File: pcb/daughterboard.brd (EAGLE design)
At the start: 28 x 24 mm, 27 parts, among them IC3 STM32F042F4, SW1 324_SW, SW2 324_SW, SW4 324_SW, SW5 324_SW, SW6 324_SW, U4 XC6206_DEV

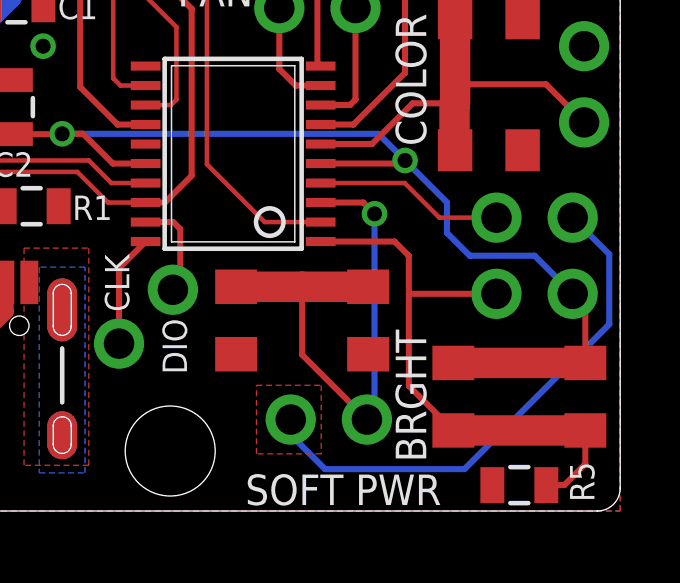
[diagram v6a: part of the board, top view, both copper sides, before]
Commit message: moved pin headers to the outer edge
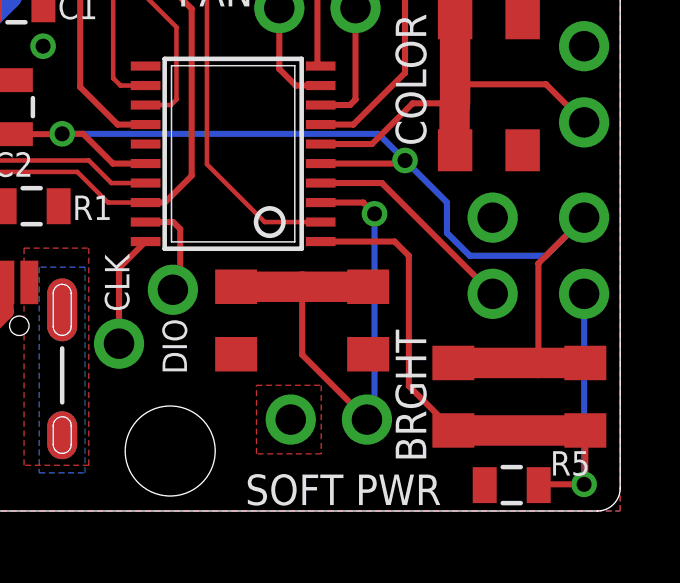
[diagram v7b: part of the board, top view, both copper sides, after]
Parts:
- moved U$4 2.08 mm to (26.8, 8.51), turned to 270 degrees
- moved U$8 1.89 mm to (23.7, 8.51), turned to 90 degrees
- moved R5 0.25 mm to (24.4, 0.86)
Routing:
- net GND: track 29.5 -> 11.8 mm
- net BUTTON2: track 19.6 -> 23.7 mm, vias 0 -> 1
- net +3V3: track 38.6 -> 42.0 mm
- net BUTTON1: track 6.34 -> 7.26 mm
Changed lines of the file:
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@@
 <attribute name="NAME" x="5.1689" y="21.3614" size="0.8128" layer="25" rot="R270"/>
 </element>
-<element name="R5" library="joyAnalog" package="0805" value="5K1" x="24.638" y="0.8636" smashed="yes">
-<attribute name="NAME" x="27.1399" y="0.3048" size="0.8128" layer="25" rot="R90"/>
+<element name="R5" library="joyAnalog" package="0805" value="5K1" x="24.384" y="0.8636" smashed="yes">
+<attribute name="NAME" x="27.0002" y="1.9939" size="0.8128" layer="25" rot="R180"/>
 </element>
 <element name="U4" library="3pos_slide_switch" package="SOT23R_INFINEON" value="XC6206_DEV" x="2.667" y="13.462" smashed="yes"/>
@@
 <element name="U$2" library="adafruit_changed" package="1X02" value="PINHD1X2" x="24.638" y="22.86" smashed="yes"/>
 <element name="U$3" library="adafruit_changed" package="1X02" value="PINHD1X2" x="26.797" y="14.224" smashed="yes" rot="R90"/>
-<element name="U$4" library="adafruit_changed" package="1X02" value="PINHD1X2" x="25.146" y="7.239" smashed="yes" rot="R180"/>
+<element name="U$4" library="adafruit_changed" package="1X02" value="PINHD1X2" x="26.797" y="8.509" smashed="yes" rot="R270"/>
 <element name="SW1" library="3pos_slide_switch_centered" package="342_SWICH_FOOT" value="324_SW" x="17.399" y="19.812" smashed="yes"/>
 <element name="SW2" library="3pos_slide_switch_centered" package="342_SWICH_FOOT" value="324_SW" x="24.638" y="19.812" smashed="yes" rot="R180"/>
@@
 <attribute name="NAME" x="4.0005" y="14.351" size="0.8128" layer="25" rot="R90"/>
 </element>
-<element name="U$8" library="adafruit_changed" package="1X02" value="PINHD1X2" x="25.146" y="9.779" smashed="yes"/>
+<element name="U$8" library="adafruit_changed" package="1X02" value="PINHD1X2" x="23.749" y="8.509" smashed="yes" rot="R90"/>
 </elements>
 <signals>
@@
 <wire x1="13.716" y1="22.86" x2="13.716" y2="20.701" width="0.1524" layer="1"/>
 <wire x1="13.716" y1="20.701" x2="15.199" y2="19.218" width="0.1524" layer="1"/>
-<wire x1="26.416" y1="9.779" x2="27.6352" y2="8.5598" width="0.2032" layer="16"/>
-<wire x1="27.6352" y1="8.5598" x2="27.6352" y2="6.223" width="0.2032" layer="16"/>
-<wire x1="27.6352" y1="6.223" x2="22.8092" y2="1.397" width="0.2032" layer="16"/>
-<wire x1="18.161" y1="1.397" x2="17.018" y2="2.54" width="0.2032" layer="16"/>
-<wire x1="17.018" y1="2.54" x2="17.018" y2="3.048" width="0.2032" layer="16"/>
-<wire x1="22.8092" y1="1.397" x2="18.161" y2="1.397" width="0.2032" layer="16"/>
 </signal>
 <signal name="+3V3">
@@
 <wire x1="20.828" y1="11.684" x2="22.225" y2="10.287" width="0.2032" layer="16"/>
 <wire x1="22.225" y1="10.287" x2="22.225" y2="9.271" width="0.2032" layer="16"/>
-<wire x1="26.838" y1="4.935" x2="22.438" y2="4.935" width="1.016" layer="1"/>
-<wire x1="26.416" y1="7.239" x2="26.838" y2="6.817" width="0.2032" layer="1"/>
-<wire x1="26.838" y1="6.817" x2="26.838" y2="4.935" width="0.2032" layer="1"/>
+<wire x1="26.838" y1="4.935" x2="25.273" y2="4.935" width="1.016" layer="1"/>
+<wire x1="25.273" y1="4.935" x2="22.438" y2="4.935" width="1.016" layer="1"/>
 <wire x1="22.225" y1="9.271" x2="22.987" y2="8.509" width="0.2032" layer="16"/>
-<wire x1="25.146" y1="8.509" x2="26.416" y2="7.239" width="0.2032" layer="16"/>
-<wire x1="22.987" y1="8.509" x2="25.146" y2="8.509" width="0.2032" layer="16"/>
+<wire x1="22.987" y1="8.509" x2="25.527" y2="8.509" width="0.2032" layer="16"/>
+<wire x1="25.527" y1="8.509" x2="26.797" y2="9.779" width="0.2032" layer="16"/>
+<wire x1="26.797" y1="9.779" x2="25.273" y2="8.255" width="0.2032" layer="1"/>
+<wire x1="25.273" y1="8.255" x2="25.273" y2="4.935" width="0.2032" layer="1"/>
 </signal>
 <signal name="USB_DP">
@@
 <contactref element="IC3" pad="4"/>
 <contactref element="U$8" pad="1"/>
-<wire x1="21.971" y1="9.779" x2="23.876" y2="9.779" width="0.1524" layer="1"/>
-<wire x1="18.0168" y1="10.932" x2="20.818" y2="10.932" width="0.1524" layer="1"/>
-<wire x1="20.818" y1="10.932" x2="21.971" y2="9.779" width="0.1524" layer="1"/>
+<wire x1="18.0168" y1="10.932" x2="20.056" y2="10.932" width="0.2032" layer="1"/>
+<wire x1="20.056" y1="10.932" x2="23.749" y2="7.239" width="0.2032" layer="1"/>
 </signal>
 <signal name="BUTTON2">
@@
 <wire x1="20.955" y1="4.168" x2="22.438" y2="2.685" width="0.2032" layer="1"/>
 <wire x1="18.0168" y1="8.982" x2="20.482" y2="8.982" width="0.2032" layer="1"/>
-<wire x1="20.955" y1="8.509" x2="20.955" y2="7.239" width="0.2032" layer="1"/>
-<wire x1="20.955" y1="7.239" x2="20.955" y2="4.168" width="0.2032" layer="1"/>
+<wire x1="20.955" y1="8.509" x2="20.955" y2="4.168" width="0.2032" layer="1"/>
 <wire x1="20.482" y1="8.982" x2="20.955" y2="8.509" width="0.2032" layer="1"/>
-<wire x1="23.876" y1="7.239" x2="20.955" y2="7.239" width="0.2032" layer="1"/>
-<wire x1="26.838" y1="2.685" x2="26.838" y2="1.565" width="0.2032" layer="1"/>
-<wire x1="26.1366" y1="0.8636" x2="25.538" y2="0.8636" width="0.2032" layer="1"/>
-<wire x1="26.838" y1="1.565" x2="26.1366" y2="0.8636" width="0.2032" layer="1"/>
+<wire x1="26.797" y1="7.239" x2="26.797" y2="0.889" width="0.2032" layer="16"/>
+<via x="26.797" y="0.889" extent="1-16" drill="0.5"/>
+<wire x1="26.797" y1="0.889" x2="25.3094" y2="0.889" width="0.2032" layer="1"/>
+<wire x1="25.3094" y1="0.889" x2="25.284" y2="0.8636" width="0.2032" layer="1"/>
+<wire x1="26.838" y1="2.685" x2="26.838" y2="0.93" width="0.2032" layer="1"/>
+<wire x1="26.838" y1="0.93" x2="26.797" y2="0.889" width="0.2032" layer="1"/>
 </signal>
 <signal name="N$29">

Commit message: freed up more space
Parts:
- moved U$2 2.96 mm to (26.8, 20.8), turned to 90 degrees
- moved SW2 1.44 mm to (23.6, 20.8), turned to 90 degrees
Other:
- board text added: "ATX4VC.com"
- board text added: "FAN SPD"
- board text added: "RGB COLOR"
- board text added: "RGB MODE"
- board text added: "dekuNukem PD1 APR23"
- board text removed: "ATX4VC.com dekuNukem"
- board text removed: "PD1 APR23"
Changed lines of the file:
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@@
 <grid distance="5" unitdist="mil" unit="mil" style="lines" multiple="1" display="no" altdistance="1" altunitdist="mil" altunit="mil"/>
 <layers>
-<layer number="1" name="Top" color="4" fill="1" visible="yes" active="yes"/>
+<layer number="1" name="Top" color="4" fill="1" visible="no" active="yes"/>
 <layer number="2" name="Route2" color="16" fill="1" visible="no" active="no"/>
 <layer number="3" name="Route3" color="17" fill="1" visible="no" active="no"/>
@@
 <layer number="19" name="Unrouted" color="6" fill="1" visible="yes" active="yes"/>
 <layer number="20" name="Dimension" color="24" fill="1" visible="yes" active="yes"/>
-<layer number="21" name="tPlace" color="7" fill="1" visible="yes" active="yes"/>
-<layer number="22" name="bPlace" color="7" fill="1" visible="yes" active="yes"/>
-<layer number="23" name="tOrigins" color="15" fill="1" visible="yes" active="yes"/>
+<layer number="21" name="tPlace" color="7" fill="1" visible="no" active="yes"/>
+<layer number="22" name="bPlace" color="7" fill="1" visible="no" active="yes"/>
+<layer number="23" name="tOrigins" color="15" fill="1" visible="no" active="yes"/>
 <layer number="24" name="bOrigins" color="15" fill="1" visible="yes" active="yes"/>
-<layer number="25" name="tNames" color="7" fill="1" visible="yes" active="yes"/>
+<layer number="25" name="tNames" color="7" fill="1" visible="no" active="yes"/>
 <layer number="26" name="bNames" color="7" fill="1" visible="yes" active="yes"/>
-<layer number="27" name="tValues" color="7" fill="1" visible="yes" active="yes"/>
-<layer number="28" name="bValues" color="7" fill="1" visible="yes" active="yes"/>
+<layer number="27" name="tValues" color="7" fill="1" visible="no" active="yes"/>
+<layer number="28" name="bValues" color="7" fill="1" visible="no" active="yes"/>
 <layer number="29" name="tStop" color="7" fill="3" visible="no" active="yes"/>
 <layer number="30" name="bStop" color="7" fill="6" visible="no" active="yes"/>
@@
 <layer number="37" name="tTest" color="7" fill="1" visible="no" active="yes"/>
 <layer number="38" name="bTest" color="7" fill="1" visible="no" active="yes"/>
-<layer number="39" name="tKeepout" color="4" fill="11" visible="yes" active="yes"/>
+<layer number="39" name="tKeepout" color="4" fill="11" visible="no" active="yes"/>
 <layer number="40" name="bKeepout" color="1" fill="11" visible="yes" active="yes"/>
-<layer number="41" name="tRestrict" color="4" fill="10" visible="yes" active="yes"/>
+<layer number="41" name="tRestrict" color="4" fill="10" visible="no" active="yes"/>
 <layer number="42" name="bRestrict" color="1" fill="10" visible="yes" active="yes"/>
 <layer number="43" name="vRestrict" color="2" fill="10" visible="no" active="yes"/>
@@
 <layer number="49" name="Reference" color="7" fill="1" visible="no" active="yes"/>
 <layer number="50" name="dxf" color="7" fill="1" visible="no" active="no"/>
-<layer number="51" name="tDocu" color="7" fill="1" visible="yes" active="yes"/>
-<layer number="52" name="bDocu" color="7" fill="1" visible="yes" active="yes"/>
+<layer number="51" name="tDocu" color="7" fill="1" visible="no" active="yes"/>
+<layer number="52" name="bDocu" color="7" fill="1" visible="no" active="yes"/>
 <layer number="53" name="tGND_GNDA" color="7" fill="1" visible="no" active="no"/>
 <layer number="54" name="bGND_GNDA" color="7" fill="1" visible="no" active="no"/>
@@
 <text x="9.92" y="15.763" size="1.778" layer="26" rot="MR180" align="center">ATX4VC
 MCU Board</text>
-<text x="21.604" y="19.928" size="1.27" layer="26" rot="MR180" align="center">ATX4VC.com
-dekuNukem</text>
 <hole x="13" y="2" drill="3" locked="yes"/>
 <circle x="13" y="2" radius="2.6" width="0" layer="41"/>
 <text x="14.5034" y="17.3274" size="1.016" layer="25" rot="R180" align="center">FAN</text>
-<text x="21.0266" y="19.9644" size="1.016" layer="25" rot="R270" align="center">MODE</text>
+<text x="21.1536" y="20.5994" size="1.016" layer="25" rot="R270" align="center">MODE</text>
 <text x="21.0266" y="14.3764" size="1.016" layer="25" rot="R270" align="center">COLOR</text>
 <text x="21.0266" y="3.8354" size="1.016" layer="25" rot="R270" align="center">BRGHT</text>
@@
 <text x="11.2314" y="7.5946" size="0.8128" layer="25" distance="10" rot="R90" align="center">CLK</text>
 <text x="13.1526" y="5.4864" size="0.8128" layer="25" distance="10" rot="R270" align="center">DIO</text>
-<text x="9.793" y="10.784" size="1.27" layer="26" rot="MR180" align="center">PD1 APR23</text>
-<text x="19.2024" y="15.2954" size="0.8128" layer="26" rot="MR180" align="center">TX</text>
-<text x="16.6624" y="15.2954" size="0.8128" layer="26" rot="MR180" align="center">DB</text>
+<text x="19.2024" y="18.3434" size="0.8128" layer="26" rot="MR180" align="center">TX</text>
+<text x="16.6624" y="18.3434" size="0.8128" layer="26" rot="MR180" align="center">DB</text>
+<text x="24.3286" y="14.3764" size="1.016" layer="26" rot="MR270" align="center">RGB
+COLOR</text>
+<text x="24.3124" y="20.9296" size="1.016" layer="26" rot="MR90" align="center">RGB
+MODE</text>
+<text x="17.4244" y="21.1374" size="1.016" layer="26" rot="MR180" align="center">FAN SPD</text>
+<text x="26.7254" y="4.0386" size="1.016" layer="26" rot="MR90" align="center">BRGHT</text>
+<text x="18.6436" y="1.0876" size="1.016" layer="26" distance="10" rot="MR0" align="center">SOFT PWR</text>
+<text x="9.892" y="10.298" size="1.27" layer="26" rot="MR0" align="center">dekuNukem
+PD1 APR23</text>
+<text x="5.348" y="0.878" size="1.27" layer="26" rot="MR180" align="center">ATX4VC.com</text>
 </plain>
 <attributes>
@@
 </element>
 <element name="U$1" library="adafruit_changed" package="1X02" value="PINHD1X2" x="17.399" y="22.86" smashed="yes"/>
-<element name="U$2" library="adafruit_changed" package="1X02" value="PINHD1X2" x="24.638" y="22.86" smashed="yes"/>
+<element name="U$2" library="adafruit_changed" package="1X02" value="PINHD1X2" x="26.797" y="20.828" smashed="yes" rot="R90"/>
 <element name="U$3" library="adafruit_changed" package="1X02" value="PINHD1X2" x="26.797" y="14.224" smashed="yes" rot="R90"/>
 <element name="U$4" library="adafruit_changed" package="1X02" value="PINHD1X2" x="26.797" y="8.509" smashed="yes" rot="R270"/>
 <element name="SW1" library="3pos_slide_switch_centered" package="342_SWICH_FOOT" value="324_SW" x="17.399" y="19.812" smashed="yes"/>
-<element name="SW2" library="3pos_slide_switch_centered" package="342_SWICH_FOOT" value="324_SW" x="24.638" y="19.812" smashed="yes" rot="R180"/>
+<element name="SW2" library="3pos_slide_switch_centered" package="342_SWICH_FOOT" value="324_SW" x="23.622" y="20.828" smashed="yes" rot="R90"/>
 <element name="SW5" library="3pos_slide_switch_centered" package="342_SWICH_FOOT" value="324_SW" x="23.622" y="14.224" smashed="yes" rot="R90"/>
 <element name="SW6" library="3pos_slide_switch_centered" package="342_SWICH_FOOT" value="324_SW" x="17.399" y="6.35" smashed="yes" rot="R180"/>
@@
 <contactref element="U$2" pad="1"/>
 <wire x1="18.0168" y1="12.882" x2="19.105" y2="12.882" width="0.2032" layer="1"/>
-<wire x1="20.828" y1="17.077" x2="22.438" y2="18.687" width="0.2032" layer="1"/>
 <wire x1="19.105" y1="12.882" x2="20.828" y2="14.605" width="0.2032" layer="1"/>
 <wire x1="20.828" y1="14.605" x2="20.828" y2="17.077" width="0.2032" layer="1"/>
-<wire x1="22.438" y1="18.687" x2="24.638" y2="18.687" width="1.016" layer="1"/>
-<wire x1="24.638" y1="18.687" x2="26.838" y2="18.687" width="1.016" layer="1"/>
-<wire x1="24.638" y1="18.687" x2="24.638" y2="21.59" width="0.2032" layer="1"/>
-<wire x1="24.638" y1="21.59" x2="23.368" y2="22.86" width="0.2032" layer="1"/>
+<wire x1="22.497" y1="23.028" x2="22.497" y2="20.828" width="1.016" layer="1"/>
+<wire x1="22.497" y1="20.828" x2="22.497" y2="18.628" width="1.016" layer="1"/>
+<wire x1="26.797" y1="19.558" x2="25.527" y2="20.828" width="0.2032" layer="1"/>
+<wire x1="25.527" y1="20.828" x2="22.497" y2="20.828" width="0.2032" layer="1"/>
+<wire x1="20.828" y1="17.077" x2="22.379" y2="18.628" width="0.2032" layer="1"/>
+<wire x1="22.379" y1="18.628" x2="22.497" y2="18.628" width="0.2032" layer="1"/>
 </signal>
 <signal name="N$11">
